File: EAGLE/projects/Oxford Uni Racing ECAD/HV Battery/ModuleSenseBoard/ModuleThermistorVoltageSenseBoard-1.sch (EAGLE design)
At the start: 12 parts

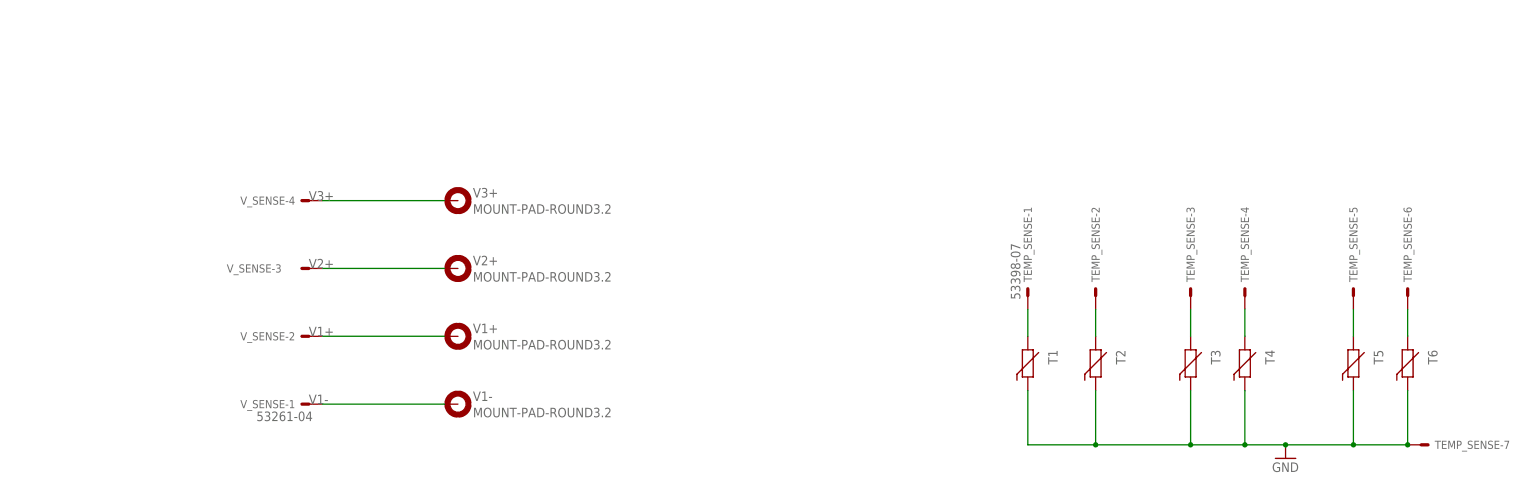
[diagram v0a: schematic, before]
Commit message: updated thermister footprint
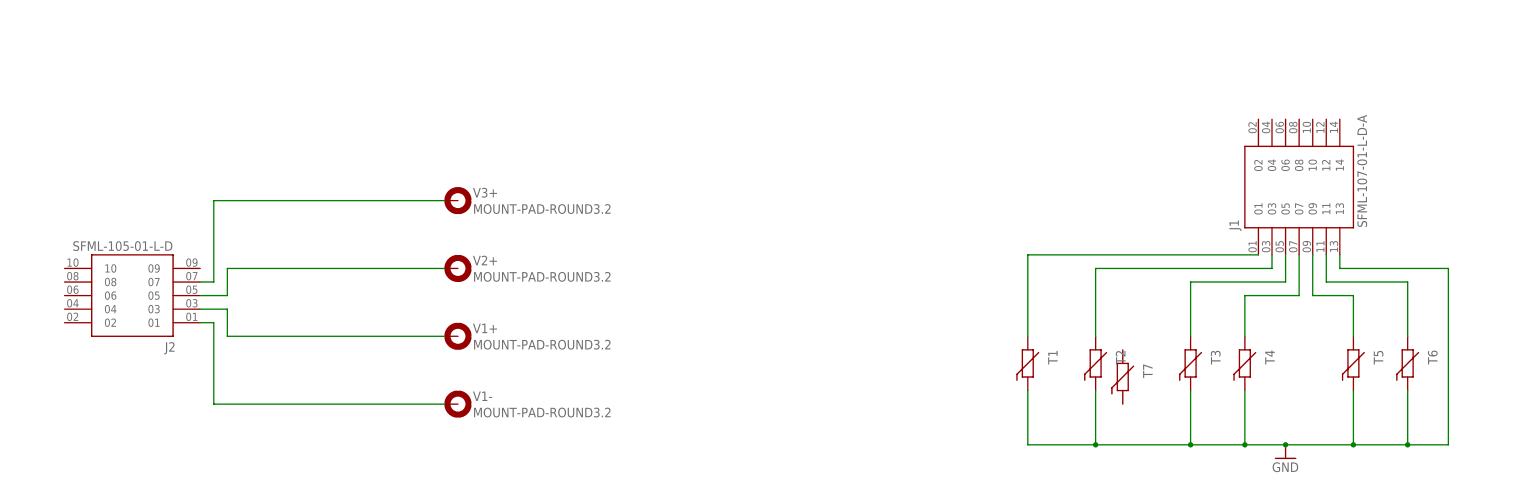
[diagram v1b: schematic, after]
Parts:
- removed TEMP_SENSE: 53398-07, con-molex:53398-07
- removed V_SENSE: 53261-04, con-molex:53261-04
- added J1: SFML-107-01-L-D-A, SFML-107-01-L-D-A:SFML-107-01-L-D-A
- added J2: SFML-105-01-L-D, SFML-105-01-L-D:SFML-105-01-L-D
- added T7: (no value), Thermistor:THERMISTOR
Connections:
- removed net N$5: T4.2, TEMP_SENSE-4.S
- removed net N$6: T5.2, TEMP_SENSE-5.S
- new net N$1: J1.07, T4.2
- new net N$2: J1.09, T5.2
- net GND: now also J1.13; no longer TEMP_SENSE-7.S
- net N$3: now also J1.03; no longer TEMP_SENSE-2.S
- net N$4: now also J1.05; no longer TEMP_SENSE-3.S
- net N$7: now also J1.11; no longer TEMP_SENSE-6.S
- net TSENSE1: now also J1.01; no longer TEMP_SENSE-1.S
- net V1+: now also J2.03; no longer V_SENSE-2.S
- net V1-: now also J2.01; no longer V_SENSE-1.S
- net V2+: now also J2.05; no longer V_SENSE-3.S
- net V3+: now also J2.07; no longer V_SENSE-4.S

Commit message: New pcb board designed to work with countersink bus bar.
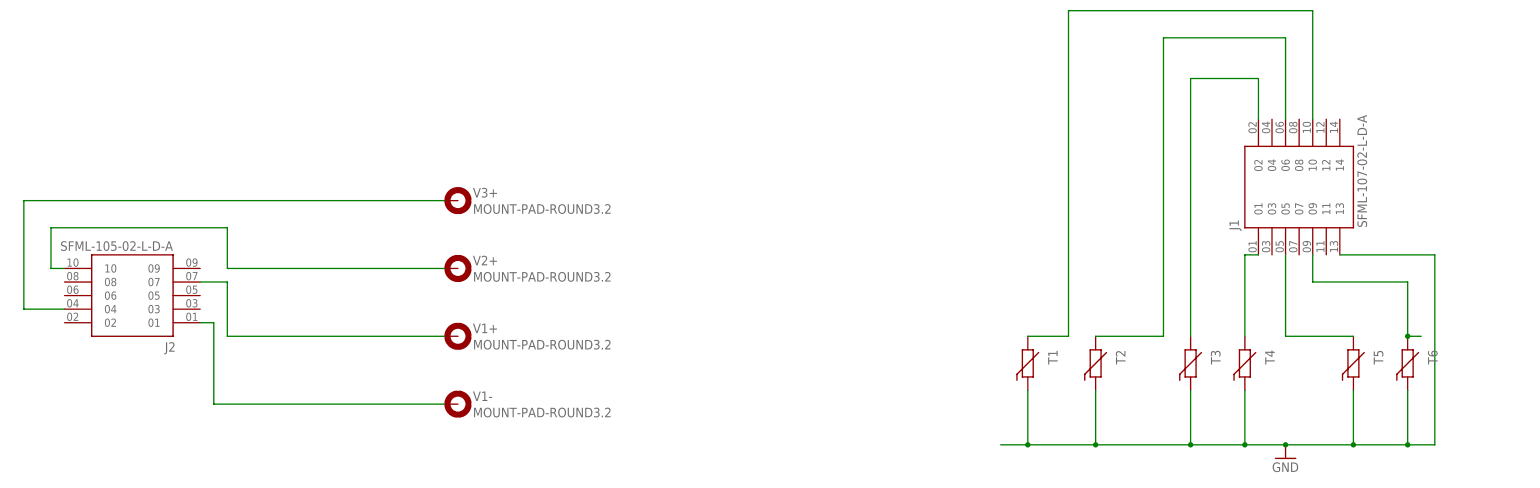
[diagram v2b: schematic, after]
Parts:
- removed T7: (no value), Thermistor:THERMISTOR
- J1: value SFML-107-01-L-D-A -> SFML-107-02-L-D-A; device SFML-107-01-L-D-A:SFML-107-01-L-D-A -> SFML-107-02-L-D-A:SFML-107-02-L-D-A
- J2: value SFML-105-01-L-D -> SFML-105-02-L-D-A; device SFML-105-01-L-D:SFML-105-01-L-D -> SFML-105-02-L-D-A:SFML-105-02-L-D-A
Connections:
- removed net N$7: J1.11, T6.2
- removed net TSENSE1: J1.01, T1.2
- new net N$5: J1.06, T2.2
- new net N$6: J1.10, T1.2
- net N$1: now also J1.05, T5.2; no longer J1.07, T4.2
- net N$2: now also T6.2; no longer T5.2
- net N$3: now also J1.01, T4.2; no longer J1.03, T2.2
- net N$4: now also J1.02; no longer J1.05
- net V1+: now also J2.07; no longer J2.03
- net V2+: now also J2.10; no longer J2.05
- net V3+: now also J2.04; no longer J2.07
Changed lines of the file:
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@@
 <part name="T6" library="Thermistor" deviceset="THERMISTOR" device=""/>
 <part name="GND1" library="supply1" library_urn="urn:adsk.eagle:library:371" deviceset="GND" device=""/>
-<part name="J1" library="SFML-107-01-L-D-A" deviceset="SFML-107-01-L-D-A" device=""/>
-<part name="J2" library="SFML-105-01-L-D" deviceset="SFML-105-01-L-D" device=""/>
-<part name="T7" library="Thermistor" deviceset="THERMISTOR" device=""/>
+<part name="J1" library="SFML-107-02-L-D-A" deviceset="SFML-107-02-L-D-A" device=""/>
+<part name="J2" library="SFML-105-02-L-D-A" deviceset="SFML-105-02-L-D-A" device=""/>
 </parts>
 <sheets>
@@
 <attribute name="VALUE" x="83.82" y="177.8" size="1.778" layer="96" rot="R180"/>
 </instance>
-<instance part="T7" gate="G$1" x="261.62" y="152.4" smashed="yes" rot="R270">
-<attribute name="NAME" x="265.43" y="154.94" size="1.778" layer="95" rot="R270"/>
-<attribute name="VALUE" x="255.27" y="154.94" size="1.778" layer="96" rot="R270"/>
-</instance>
 </instances>
 <busses>
@@
 <pinref part="GND1" gate="1" pin="GND"/>
 <junction x="292.1" y="139.7"/>
+<wire x1="243.84" y1="139.7" x2="238.76" y2="139.7" width="0.1524" layer="91"/>
+<junction x="243.84" y="139.7"/>
+<wire x1="314.96" y1="139.7" x2="320.04" y2="139.7" width="0.1524" layer="91"/>
+<wire x1="320.04" y1="139.7" x2="320.04" y2="175.26" width="0.1524" layer="91"/>
 <junction x="314.96" y="139.7"/>
-<wire x1="314.96" y1="139.7" x2="322.58" y2="139.7" width="0.1524" layer="91"/>
-<wire x1="322.58" y1="139.7" x2="322.58" y2="172.72" width="0.1524" layer="91"/>
-<wire x1="322.58" y1="172.72" x2="302.26" y2="172.72" width="0.1524" layer="91"/>
 <pinref part="J1" gate="G$1" pin="13"/>
-<wire x1="302.26" y1="172.72" x2="302.26" y2="175.26" width="0.1524" layer="91"/>
-</segment>
-</net>
-<net name="TSENSE1" class="0">
-<segment>
-<pinref part="T1" gate="G$1" pin="2"/>
-<pinref part="J1" gate="G$1" pin="01"/>
-<wire x1="243.84" y1="160.02" x2="243.84" y2="175.26" width="0.1524" layer="91"/>
-<wire x1="243.84" y1="175.26" x2="287.02" y2="175.26" width="0.1524" layer="91"/>
-</segment>
-</net>
-<net name="N$3" class="0">
-<segment>
-<pinref part="T2" gate="G$1" pin="2"/>
-<wire x1="256.54" y1="172.72" x2="256.54" y2="160.02" width="0.1524" layer="91"/>
-<wire x1="256.54" y1="172.72" x2="289.56" y2="172.72" width="0.1524" layer="91"/>
-<pinref part="J1" gate="G$1" pin="03"/>
-<wire x1="289.56" y1="172.72" x2="289.56" y2="175.26" width="0.1524" layer="91"/>
-</segment>
-</net>
-<net name="N$4" class="0">
-<segment>
-<pinref part="T3" gate="G$1" pin="2"/>
-<wire x1="274.32" y1="170.18" x2="274.32" y2="160.02" width="0.1524" layer="91"/>
-<pinref part="J1" gate="G$1" pin="05"/>
-<wire x1="274.32" y1="170.18" x2="292.1" y2="170.18" width="0.1524" layer="91"/>
-<wire x1="292.1" y1="170.18" x2="292.1" y2="175.26" width="0.1524" layer="91"/>
-</segment>
-</net>
-<net name="N$7" class="0">
-<segment>
-<pinref part="T6" gate="G$1" pin="2"/>
-<wire x1="314.96" y1="170.18" x2="314.96" y2="160.02" width="0.1524" layer="91"/>
-<wire x1="314.96" y1="170.18" x2="299.72" y2="170.18" width="0.1524" layer="91"/>
-<pinref part="J1" gate="G$1" pin="11"/>
-<wire x1="299.72" y1="170.18" x2="299.72" y2="175.26" width="0.1524" layer="91"/>
+<wire x1="320.04" y1="175.26" x2="302.26" y2="175.26" width="0.1524" layer="91"/>
 </segment>
 </net>
@@
 <segment>
 <pinref part="V3+" gate="G$1" pin="MOUNT"/>
-<wire x1="134.62" y1="185.42" x2="91.44" y2="185.42" width="0.1524" layer="91"/>
-<wire x1="91.44" y1="185.42" x2="91.44" y2="170.18" width="0.1524" layer="91"/>
-<pinref part="J2" gate="G$1" pin="07"/>
-<wire x1="91.44" y1="170.18" x2="88.9" y2="170.18" width="0.1524" layer="91"/>
+<wire x1="134.62" y1="185.42" x2="55.88" y2="185.42" width="0.1524" layer="91"/>
+<pinref part="J2" gate="G$1" pin="04"/>
+<wire x1="55.88" y1="185.42" x2="55.88" y2="165.1" width="0.1524" layer="91"/>
+<wire x1="55.88" y1="165.1" x2="63.5" y2="165.1" width="0.1524" layer="91"/>
 </segment>
 </net>
@@
 <pinref part="V2+" gate="G$1" pin="MOUNT"/>
 <wire x1="93.98" y1="172.72" x2="134.62" y2="172.72" width="0.1524" layer="91"/>
-<wire x1="93.98" y1="172.72" x2="93.98" y2="167.64" width="0.1524" layer="91"/>
-<pinref part="J2" gate="G$1" pin="05"/>
-<wire x1="93.98" y1="167.64" x2="88.9" y2="167.64" width="0.1524" layer="91"/>
+<wire x1="93.98" y1="172.72" x2="93.98" y2="180.34" width="0.1524" layer="91"/>
+<wire x1="93.98" y1="180.34" x2="60.96" y2="180.34" width="0.1524" layer="91"/>
+<pinref part="J2" gate="G$1" pin="10"/>
+<wire x1="60.96" y1="180.34" x2="60.96" y2="172.72" width="0.1524" layer="91"/>
+<wire x1="60.96" y1="172.72" x2="63.5" y2="172.72" width="0.1524" layer="91"/>
 </segment>
 </net>
@@
 <pinref part="V1+" gate="G$1" pin="MOUNT"/>
 <wire x1="134.62" y1="160.02" x2="93.98" y2="160.02" width="0.1524" layer="91"/>
-<wire x1="93.98" y1="160.02" x2="93.98" y2="165.1" width="0.1524" layer="91"/>
-<pinref part="J2" gate="G$1" pin="03"/>
-<wire x1="93.98" y1="165.1" x2="88.9" y2="165.1" width="0.1524" layer="91"/>
+<wire x1="93.98" y1="160.02" x2="93.98" y2="170.18" width="0.1524" layer="91"/>
+<pinref part="J2" gate="G$1" pin="07"/>
+<wire x1="93.98" y1="170.18" x2="88.9" y2="170.18" width="0.1524" layer="91"/>
 </segment>
 </net>
@@
 </segment>
 </net>
+<net name="N$2" class="0">
+<segment>
+<pinref part="T6" gate="G$1" pin="2"/>
+<wire x1="314.96" y1="160.02" x2="317.5" y2="160.02" width="0.1524" layer="91"/>
+<wire x1="314.96" y1="160.02" x2="314.96" y2="170.18" width="0.1524" layer="91"/>
+<wire x1="314.96" y1="170.18" x2="297.18" y2="170.18" width="0.1524" layer="91"/>
+<junction x="314.96" y="160.02"/>
+<pinref part="J1" gate="G$1" pin="09"/>
+<wire x1="297.18" y1="170.18" x2="297.18" y2="175.26" width="0.1524" layer="91"/>
+</segment>
+</net>
 <net name="N$1" class="0">
 <segment>
-<pinref part="T4" gate="G$1" pin="2"/>
-<wire x1="284.48" y1="160.02" x2="284.48" y2="167.64" width="0.1524" layer="91"/>
-<wire x1="284.48" y1="167.64" x2="294.64" y2="167.64" width="0.1524" layer="91"/>
-<pinref part="J1" gate="G$1" pin="07"/>
-<wire x1="294.64" y1="167.64" x2="294.64" y2="175.26" width="0.1524" layer="91"/>
+<pinref part="T5" gate="G$1" pin="2"/>
+<pinref part="J1" gate="G$1" pin="05"/>
+<wire x1="304.8" y1="160.02" x2="292.1" y2="160.02" width="0.1524" layer="91"/>
+<wire x1="292.1" y1="160.02" x2="292.1" y2="175.26" width="0.1524" layer="91"/>
 </segment>
 </net>
-<net name="N$2" class="0">
+<net name="N$3" class="0">
 <segment>
-<pinref part="T5" gate="G$1" pin="2"/>
-<wire x1="304.8" y1="160.02" x2="304.8" y2="167.64" width="0.1524" layer="91"/>
-<wire x1="304.8" y1="167.64" x2="297.18" y2="167.64" width="0.1524" layer="91"/>
-<pinref part="J1" gate="G$1" pin="09"/>
-<wire x1="297.18" y1="167.64" x2="297.18" y2="175.26" width="0.1524" layer="91"/>
+<pinref part="T4" gate="G$1" pin="2"/>
+<pinref part="J1" gate="G$1" pin="01"/>
+<wire x1="284.48" y1="160.02" x2="284.48" y2="175.26" width="0.1524" layer="91"/>
+<wire x1="284.48" y1="175.26" x2="287.02" y2="175.26" width="0.1524" layer="91"/>
 </segment>
 </net>
+<net name="N$4" class="0">
+<segment>
+<pinref part="T3" gate="G$1" pin="2"/>
+<wire x1="274.32" y1="160.02" x2="274.32" y2="208.28" width="0.1524" layer="91"/>
+<pinref part="J1" gate="G$1" pin="02"/>
+<wire x1="274.32" y1="208.28" x2="287.02" y2="208.28" width="0.1524" layer="91"/>
+<wire x1="287.02" y1="208.28" x2="287.02" y2="200.66" width="0.1524" layer="91"/>
+</segment>
+</net>
+<net name="N$5" class="0">
+<segment>
+<pinref part="T2" gate="G$1" pin="2"/>
+<wire x1="256.54" y1="160.02" x2="269.24" y2="160.02" width="0.1524" layer="91"/>
+<wire x1="269.24" y1="160.02" x2="269.24" y2="215.9" width="0.1524" layer="91"/>
+<pinref part="J1" gate="G$1" pin="06"/>
+<wire x1="269.24" y1="215.9" x2="292.1" y2="215.9" width="0.1524" layer="91"/>
+<wire x1="292.1" y1="215.9" x2="292.1" y2="200.66" width="0.1524" layer="91"/>
+</segment>
+</net>
+<net name="N$6" class="0">
+<segment>
+<pinref part="T1" gate="G$1" pin="2"/>
+<wire x1="243.84" y1="160.02" x2="251.46" y2="160.02" width="0.1524" layer="91"/>
+<wire x1="251.46" y1="160.02" x2="251.46" y2="220.98" width="0.1524" layer="91"/>
+<pinref part="J1" gate="G$1" pin="10"/>
+<wire x1="251.46" y1="220.98" x2="297.18" y2="220.98" width="0.1524" layer="91"/>
+<wire x1="297.18" y1="220.98" x2="297.18" y2="200.66" width="0.1524" layer="91"/>
+</segment>
+</net>
